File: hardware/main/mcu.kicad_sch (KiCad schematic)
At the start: 8 parts, among them U1 Holyiot-18010-NRF52840

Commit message: Fix footprint of the capacitors
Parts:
- C3: footprint Capacitor_SMD:C_0201_0603Metric_Pad0.64x0.40mm_HandSolder -> Capacitor_SMD:C_0603_1608Metric_Pad1.08x0.95mm_HandSolder
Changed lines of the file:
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@@
       (effects (font (size 1.27 1.27)) (justify left))
     )
-    (property "Footprint" "Capacitor_SMD:C_0201_0603Metric_Pad0.64x0.40mm_HandSolder" (id 2) (at 117.8052 36.83 0)
+    (property "Footprint" "Capacitor_SMD:C_0603_1608Metric_Pad1.08x0.95mm_HandSolder" (id 2) (at 117.8052 36.83 0)
       (effects (font (size 1.27 1.27)) hide)
     )

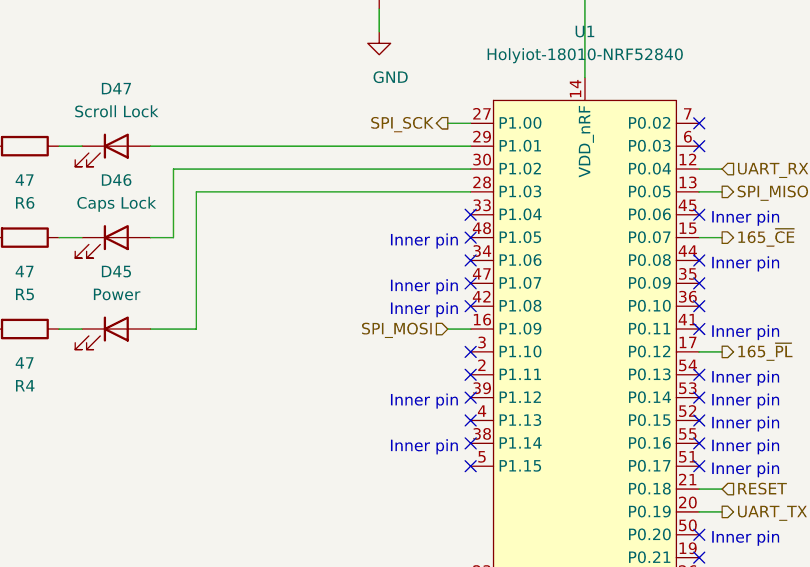
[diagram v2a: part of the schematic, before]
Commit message: Add switch to choose the connection type
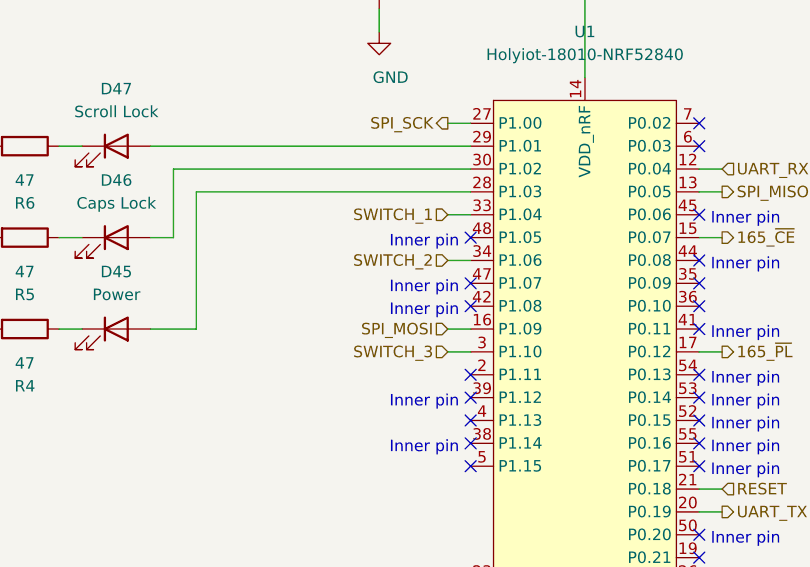
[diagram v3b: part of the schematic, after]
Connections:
- net SWITCH_3: now reaches U1.3 (P1.10)
- net SWITCH_1: now reaches U1.33 (P1.04)
- net SWITCH_2: now reaches U1.34 (P1.06)
- no-connect marks 35 -> 32
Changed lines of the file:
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@@
-(kicad_sch (version 20201015) (generator eeschema)
+(kicad_sch (version 20210123) (generator eeschema)
   (paper "A4")
   (junction (at 139.7 29.21) (diameter 1.016) (color 0 0 0 0))
   (junction (at 139.7 130.81) (diameter 1.016) (color 0 0 0 0))
-  (no_connect (at 127 59.69))
   (no_connect (at 127 62.23))
-  (no_connect (at 127 64.77))
   (no_connect (at 127 67.31))
   (no_connect (at 127 69.85))
-  (no_connect (at 127 74.93))
   (no_connect (at 127 77.47))
   (no_connect (at 127 80.01))
@@
     (stroke (width 0) (type solid) (color 0 0 0 0))
   )
+  (wire (pts (xy 124.46 59.69) (xy 127 59.69))
+    (stroke (width 0) (type solid) (color 0 0 0 0))
+  )
+  (wire (pts (xy 124.46 64.77) (xy 127 64.77))
+    (stroke (width 0) (type solid) (color 0 0 0 0))
+  )
   (wire (pts (xy 124.46 72.39) (xy 127 72.39))
     (stroke (width 0) (type solid) (color 0 0 0 0))
   )
+  (wire (pts (xy 124.46 74.93) (xy 127 74.93))
+    (stroke (width 0) (type solid) (color 0 0 0 0))
+  )
   (wire (pts (xy 124.46 100.33) (xy 127 100.33))
     (stroke (width 0) (type solid) (color 0 0 0 0))
@@
     (effects (font (size 1.27 1.27)) (justify right))
   )
+  (hierarchical_label "SWITCH_1" (shape input) (at 124.46 59.69 180)
+    (effects (font (size 1.27 1.27)) (justify right))
+  )
+  (hierarchical_label "SWITCH_2" (shape input) (at 124.46 64.77 180)
+    (effects (font (size 1.27 1.27)) (justify right))
+  )
   (hierarchical_label "SPI_MOSI" (shape input) (at 124.46 72.39 180)
     (effects (font (size 1.27 1.27)) (justify right))
   )
+  (hierarchical_label "SWITCH_3" (shape input) (at 124.46 74.93 180)
+    (effects (font (size 1.27 1.27)) (justify right))
+  )

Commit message: Fix errors found by ERC
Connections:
- net BAL_LOW: now reaches U1.2 (P1.11)
- net ~BAL_HIGH: now reaches U1.4 (P1.13)
- net ~USB_CONN: now reaches U1.5 (P1.15)
- net V_MID: now reaches U1.7 (P0.02)
- net CHARGE: now reaches U1.8 (P0.28)
- no-connect marks 32 -> 27
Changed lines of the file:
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@@
   (no_connect (at 127 67.31))
   (no_connect (at 127 69.85))
-  (no_connect (at 127 77.47))
   (no_connect (at 127 80.01))
-  (no_connect (at 127 82.55))
   (no_connect (at 127 85.09))
-  (no_connect (at 127 87.63))
-  (no_connect (at 152.4 49.53))
   (no_connect (at 152.4 52.07))
   (no_connect (at 152.4 59.69))
@@
   (no_connect (at 152.4 110.49))
   (no_connect (at 152.4 113.03))
-  (no_connect (at 152.4 115.57))
   (no_connect (at 152.4 118.11))
   (no_connect (at 152.4 120.65))
@@
     (stroke (width 0) (type solid) (color 0 0 0 0))
   )
+  (wire (pts (xy 124.46 77.47) (xy 127 77.47))
+    (stroke (width 0) (type solid) (color 0 0 0 0))
+  )
+  (wire (pts (xy 124.46 82.55) (xy 127 82.55))
+    (stroke (width 0) (type solid) (color 0 0 0 0))
+  )
+  (wire (pts (xy 124.46 87.63) (xy 127 87.63))
+    (stroke (width 0) (type solid) (color 0 0 0 0))
+  )
   (wire (pts (xy 124.46 100.33) (xy 127 100.33))
     (stroke (width 0) (type solid) (color 0 0 0 0))
@@
     (stroke (width 0) (type solid) (color 0 0 0 0))
   )
+  (wire (pts (xy 152.4 49.53) (xy 154.94 49.53))
+    (stroke (width 0) (type solid) (color 0 0 0 0))
+  )
   (wire (pts (xy 152.4 54.61) (xy 154.94 54.61))
     (stroke (width 0) (type solid) (color 0 0 0 0))
@@
     (stroke (width 0) (type solid) (color 0 0 0 0))
   )
+  (wire (pts (xy 152.4 115.57) (xy 154.94 115.57))
+    (stroke (width 0) (type solid) (color 0 0 0 0))
+  )
   (wire (pts (xy 154.94 57.15) (xy 152.4 57.15))
     (stroke (width 0) (type solid) (color 0 0 0 0))
@@
     (effects (font (size 1.27 1.27)) (justify right))
   )
+  (hierarchical_label "BAL_LOW" (shape output) (at 124.46 77.47 180)
+    (effects (font (size 1.27 1.27)) (justify right))
+  )
+  (hierarchical_label "~BAL_HIGH" (shape output) (at 124.46 82.55 180)
+    (effects (font (size 1.27 1.27)) (justify right))
+  )
+  (hierarchical_label "~USB_CONN" (shape output) (at 124.46 87.63 180)
+    (effects (font (size 1.27 1.27)) (justify right))
+  )
   (hierarchical_label "D-" (shape bidirectional) (at 124.46 100.33 180)
     (effects (font (size 1.27 1.27)) (justify right))
@@
     (effects (font (size 1.27 1.27)) (justify left))
   )
+  (hierarchical_label "V_MID" (shape input) (at 154.94 49.53 0)
+    (effects (font (size 1.27 1.27)) (justify left))
+  )
   (hierarchical_label "UART_RX" (shape input) (at 154.94 54.61 0)
     (effects (font (size 1.27 1.27)) (justify left))
@@
     (effects (font (size 1.27 1.27)) (justify left))
   )
+  (hierarchical_label "CHARGE" (shape output) (at 154.94 115.57 0)
+    (effects (font (size 1.27 1.27)) (justify left))
+  )

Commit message: Add battery voltage measurement circuit
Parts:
- added Q9: SSM3J338R, Package_TO_SOT_SMD:SOT-23_Handsoldering, symbol Device:Q_PMOS_GSD
- added R22, R23, R24: 100k, Resistor_SMD:R_0603_1608Metric_Pad0.98x0.95mm_HandSolder, symbol Device:R
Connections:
- net GND: now also R24.2
- net MEAS_V_BATT: now reaches U1.10 (P0.30)
- net MEAS_V_BATT: now also R23.2, R24.1
- net ~ACT_MEAS_V_BATT: now reaches U1.11 (P0.31)
- net ~ACT_MEAS_V_BATT: now also Q9.1 (G), R22.2
- new net: Q9.3 (D), R23.1
- new net +BATT: Q9.2 (S), R22.1
- no-connect marks 27 -> 25
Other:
- note added: "Convert the battery voltage to half its value as the MCU cannot measure it at its normal level. To prolong the battery life the voltage divider can be disconnected."
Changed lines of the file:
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@@
 (kicad_sch (version 20210123) (generator eeschema)
   (paper "A4")
+  (junction (at 41.91 151.13) (diameter 1.016) (color 0 0 0 0))
+  (junction (at 52.07 138.43) (diameter 1.016) (color 0 0 0 0))
+  (junction (at 52.07 168.91) (diameter 1.016) (color 0 0 0 0))
   (junction (at 139.7 29.21) (diameter 1.016) (color 0 0 0 0))
   (junction (at 139.7 130.81) (diameter 1.016) (color 0 0 0 0))
@@
   (no_connect (at 152.4 113.03))
   (no_connect (at 152.4 118.11))
-  (no_connect (at 152.4 120.65))
-  (no_connect (at 152.4 123.19))
+  (wire (pts (xy 20.32 151.13) (xy 41.91 151.13))
+    (stroke (width 0) (type solid) (color 0 0 0 0))
+  )
+  (wire (pts (xy 41.91 138.43) (xy 52.07 138.43))
+    (stroke (width 0) (type solid) (color 0 0 0 0))
+  )
+  (wire (pts (xy 41.91 140.97) (xy 41.91 138.43))
+    (stroke (width 0) (type solid) (color 0 0 0 0))
+  )
+  (wire (pts (xy 41.91 148.59) (xy 41.91 151.13))
+    (stroke (width 0) (type solid) (color 0 0 0 0))
+  )
+  (wire (pts (xy 41.91 151.13) (xy 44.45 151.13))
+    (stroke (width 0) (type solid) (color 0 0 0 0))
+  )
+  (wire (pts (xy 52.07 135.89) (xy 52.07 138.43))
+    (stroke (width 0) (type solid) (color 0 0 0 0))
+  )
+  (wire (pts (xy 52.07 138.43) (xy 52.07 146.05))
+    (stroke (width 0) (type solid) (color 0 0 0 0))
+  )
+  (wire (pts (xy 52.07 156.21) (xy 52.07 158.75))
+    (stroke (width 0) (type solid) (color 0 0 0 0))
+  )
+  (wire (pts (xy 52.07 166.37) (xy 52.07 168.91))
+    (stroke (width 0) (type solid) (color 0 0 0 0))
+  )
+  (wire (pts (xy 52.07 168.91) (xy 52.07 171.45))
+    (stroke (width 0) (type solid) (color 0 0 0 0))
+  )
+  (wire (pts (xy 52.07 168.91) (xy 71.12 168.91))
+    (stroke (width 0) (type solid) (color 0 0 0 0))
+  )
+  (wire (pts (xy 52.07 179.07) (xy 52.07 181.61))
+    (stroke (width 0) (type solid) (color 0 0 0 0))
+  )
   (wire (pts (xy 71.12 52.07) (xy 73.66 52.07))
     (stroke (width 0) (type solid) (color 0 0 0 0))
@@
     (stroke (width 0) (type solid) (color 0 0 0 0))
   )
+  (wire (pts (xy 152.4 120.65) (xy 170.18 120.65))
+    (stroke (width 0) (type solid) (color 0 0 0 0))
+  )
+  (wire (pts (xy 152.4 123.19) (xy 170.18 123.19))
+    (stroke (width 0) (type solid) (color 0 0 0 0))
+  )
   (wire (pts (xy 154.94 57.15) (xy 152.4 57.15))
     (stroke (width 0) (type solid) (color 0 0 0 0))
   )
+  (polyline (pts (xy 17.78 119.38) (xy 17.78 125.73))
+    (stroke (width 0) (type dash) (color 0 0 0 0))
+  )
+  (polyline (pts (xy 17.78 125.73) (xy 17.78 189.23))
+    (stroke (width 0) (type dash) (color 0 0 0 0))
+  )
+  (polyline (pts (xy 17.78 189.23) (xy 73.66 189.23))
+    (stroke (width 0) (type dash) (color 0 0 0 0))
+  )
+  (polyline (pts (xy 73.66 119.38) (xy 17.78 119.38))
+    (stroke (width 0) (type dash) (color 0 0 0 0))
+  )
+  (polyline (pts (xy 73.66 189.23) (xy 73.66 119.38))
+    (stroke (width 0) (type dash) (color 0 0 0 0))
+  )
+  (text "Convert the battery voltage to half its value as the\nMCU cannot measure it at its normal level. To prolong\nthe battery life the voltage divider can be\ndisconnected."
+    (at 19.05 129.54 0)
+    (effects (font (size 1.27 1.27)) (justify left bottom))
+  )
   (text "Inner pin" (at 125.73 63.5 180)
     (effects (font (size 1.27 1.27)) (justify right bottom))
@@
     (effects (font (size 1.27 1.27)) (justify left bottom))
   )
+  (label "~ACT_MEAS_V_BATT" (at 20.32 151.13 0)
+    (effects (font (size 1.27 1.27)) (justify left bottom))
+  )
+  (label "MEAS_V_BATT" (at 71.12 168.91 180)
+    (effects (font (size 1.27 1.27)) (justify right bottom))
+  )
+  (label "MEAS_V_BATT" (at 170.18 120.65 180)
+    (effects (font (size 1.27 1.27)) (justify right bottom))
+  )
+  (label "~ACT_MEAS_V_BATT" (at 170.18 123.19 180)
+    (effects (font (size 1.27 1.27)) (justify right bottom))
+  )
   (hierarchical_label "SPI_SCK" (shape output) (at 124.46 49.53 180)
     (effects (font (size 1.27 1.27)) (justify right))
@@
   (hierarchical_label "CHARGE" (shape output) (at 154.94 115.57 0)
     (effects (font (size 1.27 1.27)) (justify left))
+  )
+  (symbol (lib_id "power:+BATT") (at 52.07 135.89 0) (unit 1)
+    (in_bom yes) (on_board yes)
+    (property "Reference" "#PWR0145" (id 0) (at 52.07 139.7 0)
+      (effects (font (size 1.27 1.27)) hide)
+    )
+    (property "Value" "+BATT" (id 1) (at 52.4383 131.5656 0))
+    (property "Footprint" "" (id 2) (at 52.07 135.89 0)
+      (effects (font (size 1.27 1.27)) hide)
+    )
+    (property "Datasheet" "" (id 3) (at 52.07 135.89 0)
+      (effects (font (size 1.27 1.27)) hide)
+    )
+  )
+  (symbol (lib_id "power:GND") (at 52.07 181.61 0) (unit 1)
+    (in_bom yes) (on_board yes)
+    (property "Reference" "#PWR0104" (id 0) (at 52.07 187.96 0)
+      (effects (font (size 1.27 1.27)) hide)
+    )
+    (property "Value" "GND" (id 1) (at 52.1843 185.9344 0))
+    (property "Footprint" "" (id 2) (at 52.07 181.61 0)
+      (effects (font (size 1.27 1.27)) hide)
+    )
+    (property "Datasheet" "" (id 3) (at 52.07 181.61 0)
+      (effects (font (size 1.27 1.27)) hide)
+    )
   )
   (symbol (lib_id "power:GND") (at 71.12 52.07 0) (unit 1)
@@
     )
     (property "Datasheet" "" (id 3) (at 139.7 133.35 0)
+      (effects (font (size 1.27 1.27)) hide)
+    )
+  )
+  (symbol (lib_id "Device:R") (at 41.91 144.78 0) (unit 1)
+    (in_bom yes) (on_board yes)
+    (property "Reference" "R22" (id 0) (at 43.6881 143.6306 0)
+      (effects (font (size 1.27 1.27)) (justify left))
+    )
+    (property "Value" "100k" (id 1) (at 43.6881 145.9293 0)
+      (effects (font (size 1.27 1.27)) (justify left))
+    )
+    (property "Footprint" "Resistor_SMD:R_0603_1608Metric_Pad0.98x0.95mm_HandSolder" (id 2) (at 40.132 144.78 90)
+      (effects (font (size 1.27 1.27)) hide)
+    )
+    (property "Datasheet" "~" (id 3) (at 41.91 144.78 0)
+      (effects (font (size 1.27 1.27)) hide)
+    )
+  )
+  (symbol (lib_id "Device:R") (at 52.07 162.56 0) (unit 1)
+    (in_bom yes) (on_board yes)
+    (property "Reference" "R23" (id 0) (at 53.8481 161.4106 0)
+      (effects (font (size 1.27 1.27)) (justify left))
+    )
+    (property "Value" "100k" (id 1) (at 53.8481 163.7093 0)
+      (effects (font (size 1.27 1.27)) (justify left))
+    )
+    (property "Footprint" "Resistor_SMD:R_0603_1608Metric_Pad0.98x0.95mm_HandSolder" (id 2) (at 50.292 162.56 90)
+      (effects (font (size 1.27 1.27)) hide)
+    )
+    (property "Datasheet" "~" (id 3) (at 52.07 162.56 0)
+      (effects (font (size 1.27 1.27)) hide)
+    )
+  )
+  (symbol (lib_id "Device:R") (at 52.07 175.26 0) (unit 1)
+    (in_bom yes) (on_board yes)
+    (property "Reference" "R24" (id 0) (at 53.8481 174.1106 0)
+      (effects (font (size 1.27 1.27)) (justify left))
+    )
+    (property "Value" "100k" (id 1) (at 53.8481 176.4093 0)
+      (effects (font (size 1.27 1.27)) (justify left))
+    )
+    (property "Footprint" "Resistor_SMD:R_0603_1608Metric_Pad0.98x0.95mm_HandSolder" (id 2) (at 50.292 175.26 90)
+      (effects (font (size 1.27 1.27)) hide)
+    )
+    (property "Datasheet" "~" (id 3) (at 52.07 175.26 0)
       (effects (font (size 1.27 1.27)) hide)
     )
@@
       (effects (font (size 1.27 1.27)) hide)
     )
+  )
+  (symbol (lib_id "Device:Q_PMOS_GSD") (at 49.53 151.13 0) (mirror x) (unit 1)
+    (in_bom yes) (on_board yes)
+    (property "Reference" "Q9" (id 0) (at 54.7371 152.2794 0)
+      (effects (font (size 1.27 1.27)) (justify left))
+    )
+    (property "Value" "SSM3J338R" (id 1) (at 54.737 149.981 0)
+      (effects (font (size 1.27 1.27)) (justify left))
+    )
+    (property "Footprint" "Package_TO_SOT_SMD:SOT-23_Handsoldering" (id 2) (at 54.61 153.67 0)
+      (effects (font (size 1.27 1.27)) hide)
+    )
+    (property "Datasheet" "~" (id 3) (at 49.53 151.13 0)
+      (effects (font (size 1.27 1.27)) hide)
+    )
+    (property "Part Name" "Toshiba SSM3J338R" (id 4) (at 49.53 151.13 0)
+      (effects (font (size 1.27 1.27)) hide)
+    )
+    (property "Mouser" "757-SSM3J338RLF" (id 5) (at 49.53 151.13 0)
+      (effects (font (size 1.27 1.27)) hide)
+    )
